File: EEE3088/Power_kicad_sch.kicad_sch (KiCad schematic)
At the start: 27 parts, among them U1 TP4056, U2 HT7533-1

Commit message: BOM_V1_Final
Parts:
- C1, C2: JLC Part Number (none) -> C19702
- LED1: JLC Part Number (none) -> C2286
- LED2: JLC Part Number (none) -> C72043
- N-Mos1: JLC Part Number (none) -> C20917
- Op-Amp1: JLC Part Number (none) -> C7377
- P-Mos1: JLC Part Number (none) -> C15127
- R1, R4: JLC Part Number (none) -> C17398; Manufacturer_Part_Number 0402WGF1001TCE -> 0805W8F1801T5E; Price 0.0005 -> 0.0018
- R10, R4, R6, R8, R9: JLC Part Number (none) -> C17168
- R2: JLC Part Number (none) -> C22765
- R5: JLC Part Number (none) -> C17900
- R7: JLC Part Number (none) -> C17514
- U1: JLC Part Number (none) -> C16581
- U2, Voltage-Regulator-1: JLC Part Number (none) -> C14289
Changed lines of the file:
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@@
+      (effects (font (size 1.27 1.27)) hide)
+    )
+    (property "JLC Part Number" "C17514" (at 133.985 121.285 0)
       (effects (font (size 1.27 1.27)) hide)
     )
@@
     )
     (property "Description" "Voltage Regulator IC" (at 186.055 107.315 0)
+      (effects (font (size 1.27 1.27)) hide)
+    )
+    (property "JLC Part Number" "C14289" (at 186.055 107.315 0)
       (effects (font (size 1.27 1.27)) hide)
     )
@@
       (effects (font (size 1.27 1.27)) hide)
     )
+    (property "JLC Part Number" "C14289" (at 186.055 134.62 0)
+      (effects (font (size 1.27 1.27)) hide)
+    )
     (pin "1")
     (pin "2")
@@
       (effects (font (size 1.27 1.27)) hide)
     )
+    (property "JLC Part Number" "C17900" (at 38.1 143.51 0)
+      (effects (font (size 1.27 1.27)) hide)
+    )
     (pin "1")
     (pin "2")
@@
       (effects (font (size 1.27 1.27)) (justify left) hide)
     )
-    (property "Manufacturer_Part_Number" "0402WGF1001TCE" (at 88.9 40.005 0)
+    (property "Manufacturer_Part_Number" "0805W8F1801T5E" (at 88.9 40.005 0)
       (effects (font (size 1.27 1.27)) (justify left) hide)
     )
@@
       (effects (font (size 1.27 1.27)) (justify left) hide)
     )
-    (property "Price" "0.0005" (at 100.33 26.035 0)
+    (property "Price" "0.0018" (at 100.33 26.035 0)
       (effects (font (size 1.27 1.27)) hide)
     )
@@
     )
     (property "Extended" "0" (at 100.33 26.035 0)
+      (effects (font (size 1.27 1.27)) hide)
+    )
+    (property "JLC Part Number" "C17398" (at 100.33 26.035 0)
       (effects (font (size 1.27 1.27)) hide)
     )
@@
       (effects (font (size 1.27 1.27)) hide)
     )
+    (property "JLC Part Number" "C20917" (at 126.365 109.22 0)
+      (effects (font (size 1.27 1.27)) hide)
+    )
     (pin "1")
     (pin "2")
@@
     )
     (property "Price" "0.0035" (at 217.805 132.08 0)
+      (effects (font (size 1.27 1.27)) hide)
+    )
+    (property "JLC Part Number" "C17168" (at 217.805 132.08 0)
       (effects (font (size 1.27 1.27)) hide)
     )
@@
       (effects (font (size 1.27 1.27)) hide)
     )
+    (property "JLC Part Number" "C19702" (at 22.86 31.115 0)
+      (effects (font (size 1.27 1.27)) hide)
+    )
     (pin "1")
     (pin "2")
@@
       (effects (font (size 1.27 1.27)) hide)
     )
+    (property "JLC Part Number" "" (at 103.505 42.545 0)
+      (effects (font (size 1.27 1.27)) hide)
+    )
     (pin "1")
     (instances
@@
       (effects (font (size 1.27 1.27)) hide)
     )
+    (property "JLC Part Number" "C2286" (at 25.4 40.64 0)
+      (effects (font (size 1.27 1.27)) hide)
+    )
     (pin "1")
     (pin "2")
@@
       (effects (font (size 1.27 1.27)) hide)
     )
+    (property "JLC Part Number" "" (at 27.94 92.71 0)
+      (effects (font (size 1.27 1.27)) hide)
+    )
     (pin "N")
     (pin "P")
@@
       (effects (font (size 1.27 1.27)) hide)
     )
+    (property "JLC Part Number" "" (at 132.08 118.745 0)
+      (effects (font (size 1.27 1.27)) hide)
+    )
     (pin "1")
     (instances
@@
     )
     (property "Price" "0.0035" (at 218.44 104.775 0)
+      (effects (font (size 1.27 1.27)) hide)
+    )
+    (property "JLC Part Number" "C17168" (at 218.44 104.775 0)
       (effects (font (size 1.27 1.27)) hide)
     )
@@
       (effects (font (size 1.27 1.27)) hide)
     )
+    (property "JLC Part Number" "" (at 206.375 132.08 0)
+      (effects (font (size 1.27 1.27)) hide)
+    )
     (pin "1")
     (instances
@@
     )
     (property "Price" "0.0035" (at 137.16 118.745 0)
+      (effects (font (size 1.27 1.27)) hide)
+    )
+    (property "JLC Part Number" "C17168" (at 137.16 118.745 0)
       (effects (font (size 1.27 1.27)) hide)
     )
@@
       (effects (font (size 1.27 1.27)) hide)
     )
+    (property "JLC Part Number" "C19702" (at 88.265 53.34 0)
+      (effects (font (size 1.27 1.27)) hide)
+    )
     (pin "1")
     (pin "2")
@@
       (effects (font (size 1.27 1.27)) hide)
     )
+    (property "JLC Part Number" "C17168" (at 115.57 42.545 0)
+      (effects (font (size 1.27 1.27)) hide)
+    )
     (pin "1")
     (pin "2")
@@
       (effects (font (size 1.27 1.27)) hide)
     )
+    (property "JLC Part Number" "" (at 205.74 104.775 0)
+      (effects (font (size 1.27 1.27)) hide)
+    )
     (pin "1")
     (instances
@@
     )
     (property "Price" "0.0035" (at 55.245 109.22 0)
+      (effects (font (size 1.27 1.27)) hide)
+    )
+    (property "JLC Part Number" "C17168" (at 55.245 109.22 0)
       (effects (font (size 1.27 1.27)) hide)
     )
@@
     )
     (property "Manufacturer_Part_Number" "TP4056-42-ESOP8" (at 66.675 47.625 0)
+      (effects (font (size 1.27 1.27)) hide)
+    )
+    (property "JLC Part Number" "C16581" (at 66.675 47.625 0)
       (effects (font (size 1.27 1.27)) hide)
     )
@@
       (effects (font (size 1.27 1.27)) hide)
     )
+    (property "JLC Part Number" "C72043" (at 100.33 24.765 0)
+      (effects (font (size 1.27 1.27)) hide)
+    )
     (pin "1")
     (pin "2")
@@
       (effects (font (size 1.27 1.27)) (justify left) hide)
     )
-    (property "Manufacturer_Part_Number" "0402WGF1001TCE" (at 11.43 60.96 0)
+    (property "Manufacturer_Part_Number" "0805W8F1801T5E" (at 11.43 60.96 0)
       (effects (font (size 1.27 1.27)) (justify left) hide)
     )
@@
       (effects (font (size 1.27 1.27)) (justify left) hide)
     )
-    (property "Price" "0.0005" (at 22.86 46.99 0)
+    (property "Price" "0.0018" (at 22.86 46.99 0)
       (effects (font (size 1.27 1.27)) hide)
     )
@@
     )
     (property "Extended" "0" (at 22.86 46.99 0)
+      (effects (font (size 1.27 1.27)) hide)
+    )
+    (property "JLC Part Number" "C17398" (at 22.86 46.99 0)
       (effects (font (size 1.27 1.27)) hide)
     )
@@
       (effects (font (size 1.27 1.27)) hide)
     )
+    (property "JLC Part Number" "" (at 44.45 109.22 0)
+      (effects (font (size 1.27 1.27)) hide)
+    )
     (pin "1")
     (instances
@@
       (effects (font (size 1.27 1.27)) hide)
     )
+    (property "JLC Part Number" "" (at 48.26 118.11 0)
+      (effects (font (size 1.27 1.27)) hide)
+    )
     (pin "A")
     (pin "C")
@@
       (effects (font (size 1.27 1.27)) hide)
     )
+    (property "JLC Part Number" "C15127" (at 38.1 116.84 0)
+      (effects (font (size 1.27 1.27)) hide)
+    )
     (pin "1")
     (pin "2")
@@
     )
     (property "Extended" "0" (at 93.98 109.22 0)
+      (effects (font (size 1.27 1.27)) hide)
+    )
+    (property "JLC Part Number" "C7377" (at 93.98 109.22 0)
       (effects (font (size 1.27 1.27)) hide)
     )
@@
       (effects (font (size 1.27 1.27)) hide)
     )
+    (property "JLC Part Number" "C22765" (at 29.845 50.165 0)
+      (effects (font (size 1.27 1.27)) hide)
+    )

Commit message: Update Power_kicad_sch.kicad_sch
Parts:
- added TP22: TestPoint, symbol Connector:TestPoint
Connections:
- net at N-Mos1.1, Op-Amp1.1 (VOUTA): now also TP22.1
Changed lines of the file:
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@@
   (junction (at 205.74 104.775) (diameter 0) (color 0 0 0 0)
+  )
+  (junction (at 124.46 109.22) (diameter 0) (color 0 0 0 0)
   )
   (junction (at 103.505 42.545) (diameter 0) (color 0 0 0 0)
@@
         )
       )
+    )
+  )
+  (symbol (lib_id "Connector:TestPoint") (at 124.46 109.22 0) (unit 1)
+    (in_bom yes) (on_board yes) (dnp no) (fields_autoplaced)
+    (property "Reference" "TP22" (at 127 105.283 0)
+      (effects (font (size 1.27 1.27)) (justify left))
+    )
+    (property "Value" "TestPoint" (at 127 107.823 0)
+      (effects (font (size 1.27 1.27)) (justify left))
+    )
+    (property "Footprint" "" (at 129.54 109.22 0)
+      (effects (font (size 1.27 1.27)) hide)
+    )
+    (property "Datasheet" "~" (at 129.54 109.22 0)
+      (effects (font (size 1.27 1.27)) hide)
+    )
+    (pin "1")
+    (instances
+      (project "EEE3088"
+        (path "/83bdd5e1-981a-4ca1-9a2f-70dea9f00850/1213f935-6f8d-4a20-9c2e-6b5e9a834fe6"
+          (reference "TP22") (unit 1)
+        )
+      )

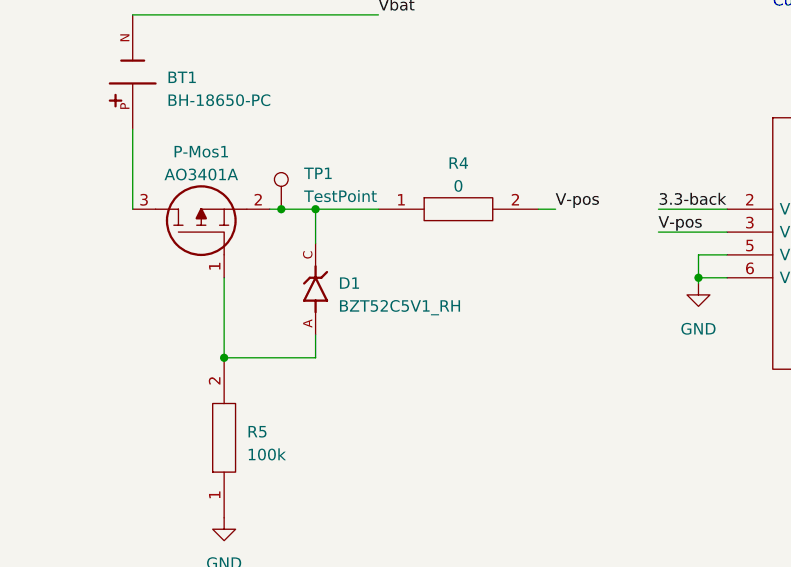
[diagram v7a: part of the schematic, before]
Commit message: Power - zener
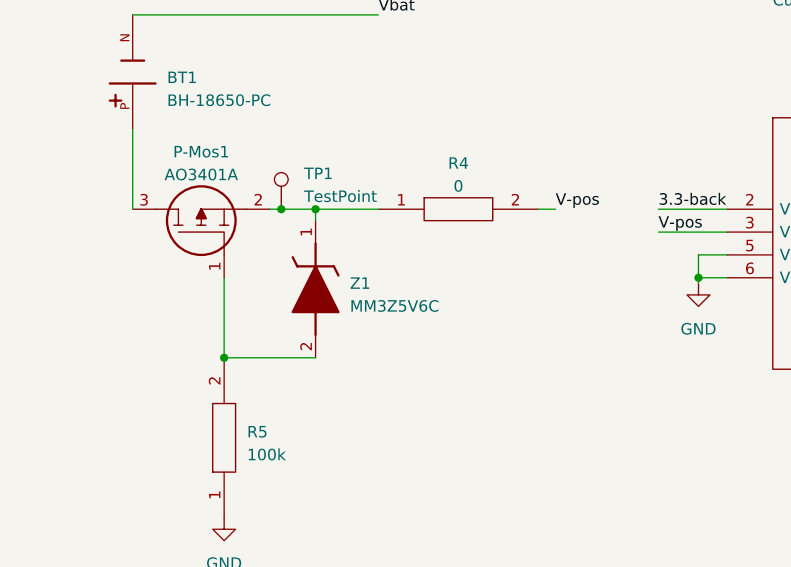
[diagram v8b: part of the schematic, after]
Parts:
- removed D1: BZT52C5V1_RH, DIO_BZT52C5V1_RH, symbol BZT52C5V1_RH:BZT52C5V1_RH
- added Z1: MM3Z5V6C, SODFL2513X100N, symbol MM3Z5V6C:MM3Z5V6C
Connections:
- net at P-Mos1.1, R5.2: now also Z1.2 (A)
- net at P-Mos1.2, R4.1, TP1.1: now also Z1.1 (K)
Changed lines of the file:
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@@
+    (stroke (width 0) (type default))
+  )
+  (wire (pts (xy 48.26 109.22) (xy 55.245 109.22))
     (stroke (width 0) (type default))
   )
@@
     (stroke (width 0) (type default))
   )
-  (wire (pts (xy 48.26 123.19) (xy 48.26 125.73))
-    (stroke (width 0) (type default))
-  )
   (wire (pts (xy 40.64 24.765) (xy 48.895 24.765))
     (stroke (width 0) (type default))
@@
     (stroke (width 0) (type default))
   )
-  (wire (pts (xy 48.26 109.22) (xy 55.245 109.22))
-    (stroke (width 0) (type default))
-  )
   (wire (pts (xy 40.64 24.765) (xy 22.86 24.765))
     (stroke (width 0) (type default))
@@
     (stroke (width 0) (type default))
   )
-  (wire (pts (xy 48.26 109.22) (xy 48.26 113.03))
-    (stroke (width 0) (type default))
-  )
   (wire (pts (xy 22.86 24.765) (xy 22.86 26.035))
     (stroke (width 0) (type default))
@@
   )
   (wire (pts (xy 90.805 116.84) (xy 90.805 117.475))
+    (stroke (width 0) (type default))
+  )
+  (wire (pts (xy 48.26 109.22) (xy 48.26 110.49))
     (stroke (width 0) (type default))
   )
@@
         (path "/83bdd5e1-981a-4ca1-9a2f-70dea9f00850/1213f935-6f8d-4a20-9c2e-6b5e9a834fe6"
           (reference "C1") (unit 1)
+        )
+      )
+    )
+  )
+  (symbol (lib_id "MM3Z5V6C:MM3Z5V6C") (at 48.26 110.49 270) (unit 1)
+    (in_bom yes) (on_board yes) (dnp no) (fields_autoplaced)
+    (property "Reference" "Z1" (at 52.07 117.475 90)
+      (effects (font (size 1.27 1.27)) (justify left))
+    )
+    (property "Value" "MM3Z5V6C" (at 52.07 120.015 90)
+      (effects (font (size 1.27 1.27)) (justify left))
+    )
+    (property "Footprint" "SODFL2513X100N" (at -45.39 120.65 0)
+      (effects (font (size 1.27 1.27)) (justify left top) hide)
+    )
+    (property "Datasheet" "https://ms.componentsearchengine.com/Datasheets/2/MM3Z5V6C.pdf" (at -145.39 120.65 0)
+      (effects (font (size 1.27 1.27)) (justify left top) hide)
+    )
+    (property "Height" "1" (at -345.39 120.65 0)
+      (effects (font (size 1.27 1.27)) (justify left top) hide)
+    )
+    (property "Manufacturer_Name" "onsemi" (at -445.39 120.65 0)
+      (effects (font (size 1.27 1.27)) (justify left top) hide)
+    )
+    (property "Manufacturer_Part_Number" "MM3Z5V6C" (at -545.39 120.65 0)
+      (effects (font (size 1.27 1.27)) (justify left top) hide)
+    )
+    (property "Mouser Part Number" "512-MM3Z5V6C" (at -645.39 120.65 0)
+      (effects (font (size 1.27 1.27)) (justify left top) hide)
+    )
+    (property "Mouser Price/Stock" "https://www.mouser.co.uk/ProductDetail/onsemi-Fairchild/MM3Z5V6C?qs=rXqtSHp76q6mZxise9dftg%3D%3D" (at -745.39 120.65 0)
+      (effects (font (size 1.27 1.27)) (justify left top) hide)
+    )
+    (property "Arrow Part Number" "MM3Z5V6C" (at -845.39 120.65 0)
+      (effects (font (size 1.27 1.27)) (justify left top) hide)
+    )
+    (property "Arrow Price/Stock" "https://www.arrow.com/en/products/mm3z5v6c/on-semiconductor?region=nac" (at -945.39 120.65 0)
+      (effects (font (size 1.27 1.27)) (justify left top) hide)
+    )
+    (property "Description" "Zener" (at 48.26 110.49 0)
+      (effects (font (size 1.27 1.27)) hide)
+    )
+    (property "Extended" "1" (at 48.26 110.49 0)
+      (effects (font (size 1.27 1.27)) hide)
+    )
+    (property "JLC Part Number" "C48886" (at 48.26 110.49 0)
+      (effects (font (size 1.27 1.27)) hide)
+    )
+    (property "Price" "0.0184" (at 48.26 110.49 0)
+      (effects (font (size 1.27 1.27)) hide)
+    )
+    (pin "1")
+    (pin "2")
+    (instances
+      (project "EEE3088"
+        (path "/83bdd5e1-981a-4ca1-9a2f-70dea9f00850/1213f935-6f8d-4a20-9c2e-6b5e9a834fe6"
+          (reference "Z1") (unit 1)
         )
       )
@@
         )
       )
-    )
-  )
-  (symbol (lib_id "BZT52C5V1_RH:BZT52C5V1_RH") (at 48.26 118.11 90) (unit 1)
-    (in_bom yes) (on_board yes) (dnp no) (fields_autoplaced)
-    (property "Reference" "D1" (at 50.8 117.475 90)
-      (effects (font (size 1.27 1.27)) (justify right))
-    )
-    (property "Value" "BZT52C5V1_RH" (at 50.8 120.015 90)
-      (effects (font (size 1.27 1.27)) (justify right))
-    )
-    (property "Footprint" "DIO_BZT52C5V1_RH" (at 48.26 118.11 0)
-      (effects (font (size 1.27 1.27)) (justify bottom) hide)
-    )
-    (property "Datasheet" "-" (at 48.26 118.11 0)
-      (effects (font (size 1.27 1.27)) hide)
-    )
-    (property "STANDARD" "Manufacturer Recommendations" (at 48.26 118.11 0)
-      (effects (font (size 1.27 1.27)) (justify bottom) hide)
-    )
-    (property "MANUFACTURER" "Taiwan Semiconductor" (at 48.26 118.11 0)
-      (effects (font (size 1.27 1.27)) (justify bottom) hide)
-    )
-    (property "PARTREV" "F15" (at 48.26 118.11 0)
-      (effects (font (size 1.27 1.27)) (justify bottom) hide)
-    )
-    (property "MAXIMUM_PACKAGE_HEIGHT" "1.15 mm" (at 48.26 118.11 0)
-      (effects (font (size 1.27 1.27)) (justify bottom) hide)
-    )
-    (property "Price" "-" (at 48.26 118.11 0)
-      (effects (font (size 1.27 1.27)) hide)
-    )
-    (property "Basic" "" (at 48.26 118.11 0)
-      (effects (font (size 1.27 1.27)) hide)
-    )
-    (property "Extended" "0" (at 48.26 118.11 0)
-      (effects (font (size 1.27 1.27)) hide)
-    )
-    (property "Description" "Zener Diode" (at 48.26 118.11 0)
-      (effects (font (size 1.27 1.27)) hide)
-    )
-    (property "Manufacturer_Part_Number" "-" (at 48.26 118.11 0)
-      (effects (font (size 1.27 1.27)) hide)
-    )
-    (property "JLC Part Number" "" (at 48.26 118.11 0)
-      (effects (font (size 1.27 1.27)) hide)
-    )
-    (pin "A")
-    (pin "C")
-    (instances
-      (project "Power_kicad_sch"
-        (path "/02e53f89-135a-4459-982b-e3c28e008824"
-          (reference "D1") (unit 1)
-        )
-      )
-      (project "EEE3088"
-        (path "/83bdd5e1-981a-4ca1-9a2f-70dea9f00850/1213f935-6f8d-4a20-9c2e-6b5e9a834fe6"
-          (reference "D1") (unit 1)
-        )
-      )
